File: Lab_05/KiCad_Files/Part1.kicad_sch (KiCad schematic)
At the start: 9 parts, among them Q10 NPN

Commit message: Continue Lab 5
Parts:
- added R115: 100R, symbol Device:R
- added V102: 15V, symbol Simulation_SPICE:VDC
- C103: renamed from C3; value C -> 1uF; symbol Device:C -> Device:C_Polarized_US
- C104: renamed from C4; value 40C -> 47uF; symbol Device:C -> Device:C_Polarized_US
- L101: renamed from L1; value L -> 4mH
- R116: renamed from R15; value R -> 10K
- R117: renamed from R16; value R -> 1K
- R118: renamed from R18; value 24R -> 2K7
- R119: renamed from R17; value R -> 100R
- V1: value VSIN -> VSIN_P1
- renumbered Q10 to Q110
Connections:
- net +15V: now also V102.1
- net GND: now also V102.2
- net at Q110.2 (B), R116.2, R117.1: now also C104.1; no longer C104.2
- net at C103.1, L101.1: now also C104.2, R115.2; no longer C104.1, V1.1
- new net: R115.1, V1.1
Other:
- note added: ".ac dec 100 1 10Meg"
- company: (none) -> Jim Horwitz & Mark Vaughn, Jork Incorporated
- title: (none) -> Single-Transistor Bandpass Amplifier
- moved on the sheet: L101, Q110, R116, R117, R118, R119

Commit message: Finish Saturday Schematics
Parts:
- renumbered C103 to C357, C104 to C358, L101 to L353, Q110 to Q362, R115 to R377, R116 to R378, R117 to R379, R118 to R380, R119 to R381, V102 to V353
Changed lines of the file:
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@@
   (symbol (lib_id "Device:R") (at 116.84 72.39 0) (unit 1)
     (in_bom yes) (on_board yes) (dnp no) (fields_autoplaced)
-    (property "Reference" "R117" (at 119.38 71.12 0)
+    (property "Reference" "R379" (at 119.38 71.12 0)
       (effects (font (size 1.27 1.27)) (justify left))
     )
@@
       (project "Lab05"
         (path "/9fa84b6a-7d78-4b93-9106-2eb97c609eaa/a137afc5-afed-494e-bb1a-b2a03cb8cb70"
-          (reference "R117") (unit 1)
+          (reference "R379") (unit 1)
         )
       )
@@
         )
         (path "/9fa84b6a-7d78-4b93-9106-2eb97c609eaa/a137afc5-afed-494e-bb1a-b2a03cb8cb70"
-          (reference "#PWR0126") (unit 1)
+          (reference "#PWR0389") (unit 1)
         )
       )
@@
   (symbol (lib_id "Device:R") (at 132.08 76.2 0) (unit 1)
     (in_bom yes) (on_board yes) (dnp no) (fields_autoplaced)
-    (property "Reference" "R119" (at 134.62 74.93 0)
+    (property "Reference" "R381" (at 134.62 74.93 0)
       (effects (font (size 1.27 1.27)) (justify left))
     )
@@
       (project "Lab05"
         (path "/9fa84b6a-7d78-4b93-9106-2eb97c609eaa/a137afc5-afed-494e-bb1a-b2a03cb8cb70"
-          (reference "R119") (unit 1)
+          (reference "R381") (unit 1)
         )
       )
@@
         )
         (path "/9fa84b6a-7d78-4b93-9106-2eb97c609eaa/a137afc5-afed-494e-bb1a-b2a03cb8cb70"
-          (reference "#PWR0128") (unit 1)
+          (reference "#PWR0391") (unit 1)
         )
       )
@@
         )
         (path "/9fa84b6a-7d78-4b93-9106-2eb97c609eaa/a137afc5-afed-494e-bb1a-b2a03cb8cb70"
-          (reference "V103") (unit 1)
+          (reference "V354") (unit 1)
         )
       )
@@
   (symbol (lib_id "Simulation_SPICE:VDC") (at 26.67 111.76 0) (unit 1)
     (in_bom yes) (on_board yes) (dnp no) (fields_autoplaced)
-    (property "Reference" "V102" (at 30.48 110.4542 0)
+    (property "Reference" "V353" (at 30.48 110.4542 0)
       (effects (font (size 1.27 1.27)) (justify left))
     )
@@
       (project "Lab05"
         (path "/9fa84b6a-7d78-4b93-9106-2eb97c609eaa/a137afc5-afed-494e-bb1a-b2a03cb8cb70"
-          (reference "V102") (unit 1)
+          (reference "V353") (unit 1)
         )
       )
@@
         )
         (path "/9fa84b6a-7d78-4b93-9106-2eb97c609eaa/a137afc5-afed-494e-bb1a-b2a03cb8cb70"
-          (reference "#PWR0130") (unit 1)
+          (reference "#PWR0393") (unit 1)
         )
       )
@@
         )
         (path "/9fa84b6a-7d78-4b93-9106-2eb97c609eaa/a137afc5-afed-494e-bb1a-b2a03cb8cb70"
-          (reference "#PWR0123") (unit 1)
+          (reference "#PWR0386") (unit 1)
         )
       )
@@
         )
         (path "/9fa84b6a-7d78-4b93-9106-2eb97c609eaa/a137afc5-afed-494e-bb1a-b2a03cb8cb70"
-          (reference "#PWR0124") (unit 1)
+          (reference "#PWR0387") (unit 1)
         )
       )
@@
   (symbol (lib_id "Device:R") (at 76.2 66.04 90) (unit 1)
     (in_bom yes) (on_board yes) (dnp no)
-    (property "Reference" "R115" (at 76.2 63.5 90)
+    (property "Reference" "R377" (at 76.2 63.5 90)
       (effects (font (size 1.27 1.27)))
     )
@@
       (project "Lab05"
         (path "/9fa84b6a-7d78-4b93-9106-2eb97c609eaa/a137afc5-afed-494e-bb1a-b2a03cb8cb70"
-          (reference "R115") (unit 1)
+          (reference "R377") (unit 1)
         )
       )
@@
   (symbol (lib_id "Device:C_Polarized_US") (at 96.52 72.39 0) (unit 1)
     (in_bom yes) (on_board yes) (dnp no) (fields_autoplaced)
-    (property "Reference" "C103" (at 100.33 71.12 0)
+    (property "Reference" "C357" (at 100.33 71.12 0)
       (effects (font (size 1.27 1.27)) (justify left))
     )
@@
       (project "Lab05"
         (path "/9fa84b6a-7d78-4b93-9106-2eb97c609eaa/a137afc5-afed-494e-bb1a-b2a03cb8cb70"
-          (reference "C103") (unit 1)
+          (reference "C357") (unit 1)
         )
       )
@@
   (symbol (lib_id "Device:L") (at 85.09 72.39 0) (unit 1)
     (in_bom yes) (on_board yes) (dnp no) (fields_autoplaced)
-    (property "Reference" "L101" (at 86.36 71.12 0)
+    (property "Reference" "L353" (at 86.36 71.12 0)
       (effects (font (size 1.27 1.27)) (justify left))
     )
@@
       (project "Lab05"
         (path "/9fa84b6a-7d78-4b93-9106-2eb97c609eaa/a137afc5-afed-494e-bb1a-b2a03cb8cb70"
-          (reference "L101") (unit 1)
+          (reference "L353") (unit 1)
         )
       )
@@
         )
         (path "/9fa84b6a-7d78-4b93-9106-2eb97c609eaa/a137afc5-afed-494e-bb1a-b2a03cb8cb70"
-          (reference "#PWR0125") (unit 1)
+          (reference "#PWR0388") (unit 1)
         )
       )
@@
   (symbol (lib_id "power:+15V") (at 26.67 102.87 0) (unit 1)
     (in_bom yes) (on_board yes) (dnp no) (fields_autoplaced)
-    (property "Reference" "#PWR0122" (at 26.67 106.68 0)
+    (property "Reference" "#PWR0385" (at 26.67 106.68 0)
       (effects (font (size 1.27 1.27)) hide)
     )
@@
       (project "Lab05"
         (path "/9fa84b6a-7d78-4b93-9106-2eb97c609eaa/a137afc5-afed-494e-bb1a-b2a03cb8cb70"
-          (reference "#PWR0122") (unit 1)
+          (reference "#PWR0385") (unit 1)
         )
       )
@@
   (symbol (lib_id "power:+15V") (at 116.84 52.07 0) (unit 1)
     (in_bom yes) (on_board yes) (dnp no) (fields_autoplaced)
-    (property "Reference" "#PWR0127" (at 116.84 55.88 0)
+    (property "Reference" "#PWR0390" (at 116.84 55.88 0)
       (effects (font (size 1.27 1.27)) hide)
     )
@@
       (project "Lab05"
         (path "/9fa84b6a-7d78-4b93-9106-2eb97c609eaa/a137afc5-afed-494e-bb1a-b2a03cb8cb70"
-          (reference "#PWR0127") (unit 1)
+          (reference "#PWR0390") (unit 1)
         )
       )
@@
   (symbol (lib_id "Simulation_SPICE:NPN") (at 129.54 66.04 0) (unit 1)
     (in_bom yes) (on_board yes) (dnp no) (fields_autoplaced)
-    (property "Reference" "Q110" (at 134.62 64.77 0)
+    (property "Reference" "Q362" (at 134.62 64.77 0)
       (effects (font (size 1.27 1.27)) (justify left))
     )
@@
       (project "Lab05"
         (path "/9fa84b6a-7d78-4b93-9106-2eb97c609eaa/a137afc5-afed-494e-bb1a-b2a03cb8cb70"
-          (reference "Q110") (unit 1)
+          (reference "Q362") (unit 1)
         )
       )
@@
   (symbol (lib_id "Device:C_Polarized_US") (at 107.95 66.04 270) (mirror x) (unit 1)
     (in_bom yes) (on_board yes) (dnp no)
-    (property "Reference" "C104" (at 107.95 58.42 90)
+    (property "Reference" "C358" (at 107.95 58.42 90)
       (effects (font (size 1.27 1.27)))
     )
@@
       (project "Lab05"
         (path "/9fa84b6a-7d78-4b93-9106-2eb97c609eaa/a137afc5-afed-494e-bb1a-b2a03cb8cb70"
-          (reference "C104") (unit 1)
+          (reference "C358") (unit 1)
         )
       )
@@
   (symbol (lib_id "Device:R") (at 132.08 54.61 0) (unit 1)
     (in_bom yes) (on_board yes) (dnp no) (fields_autoplaced)
-    (property "Reference" "R118" (at 134.62 53.34 0)
+    (property "Reference" "R380" (at 134.62 53.34 0)
       (effects (font (size 1.27 1.27)) (justify left))
     )
@@
       (project "Lab05"
         (path "/9fa84b6a-7d78-4b93-9106-2eb97c609eaa/a137afc5-afed-494e-bb1a-b2a03cb8cb70"
-          (reference "R118") (unit 1)
+          (reference "R380") (unit 1)
         )
       )
@@
   (symbol (lib_id "Device:R") (at 116.84 57.15 0) (unit 1)
     (in_bom yes) (on_board yes) (dnp no) (fields_autoplaced)
-    (property "Reference" "R116" (at 119.38 55.88 0)
+    (property "Reference" "R378" (at 119.38 55.88 0)
       (effects (font (size 1.27 1.27)) (justify left))
     )
@@
       (project "Lab05"
         (path "/9fa84b6a-7d78-4b93-9106-2eb97c609eaa/a137afc5-afed-494e-bb1a-b2a03cb8cb70"
-          (reference "R116") (unit 1)
+          (reference "R378") (unit 1)
         )
       )
@@
   (symbol (lib_id "power:+15V") (at 132.08 49.53 0) (unit 1)
     (in_bom yes) (on_board yes) (dnp no) (fields_autoplaced)
-    (property "Reference" "#PWR0129" (at 132.08 53.34 0)
+    (property "Reference" "#PWR0392" (at 132.08 53.34 0)
       (effects (font (size 1.27 1.27)) hide)
     )
@@
       (project "Lab05"
         (path "/9fa84b6a-7d78-4b93-9106-2eb97c609eaa/a137afc5-afed-494e-bb1a-b2a03cb8cb70"
-          (reference "#PWR0129") (unit 1)
-        )
-      )
+          (reference "#PWR0392") (unit 1)
+        )
+      )

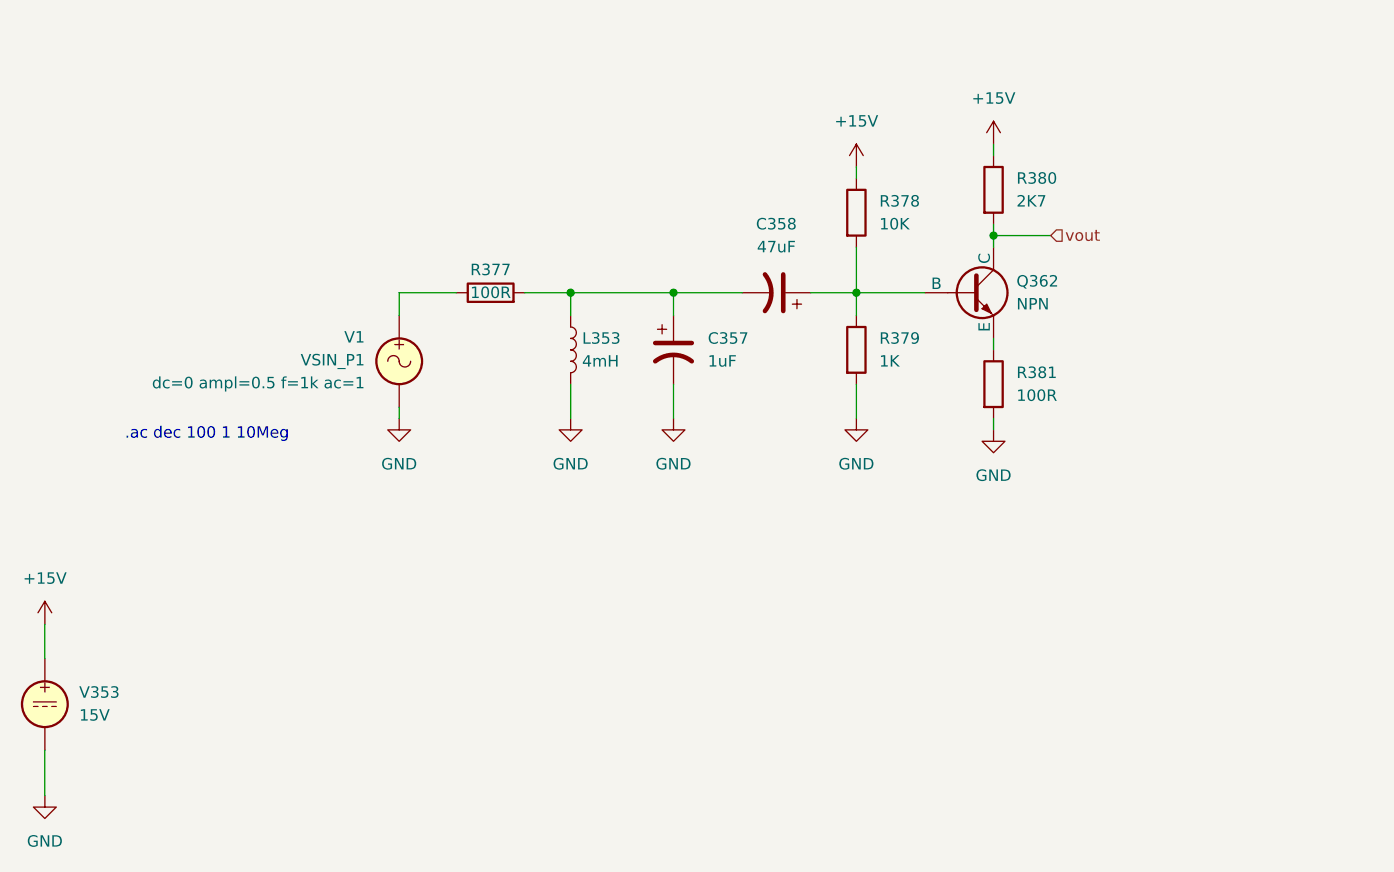
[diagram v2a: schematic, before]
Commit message: Revise part 3 Version 1
For next revision:
- add collector resistor to Q304
- remove R309
- add emitter follower after integrator
For the future:
- add more poles to bandpass!!
- maybe a resonant filter?
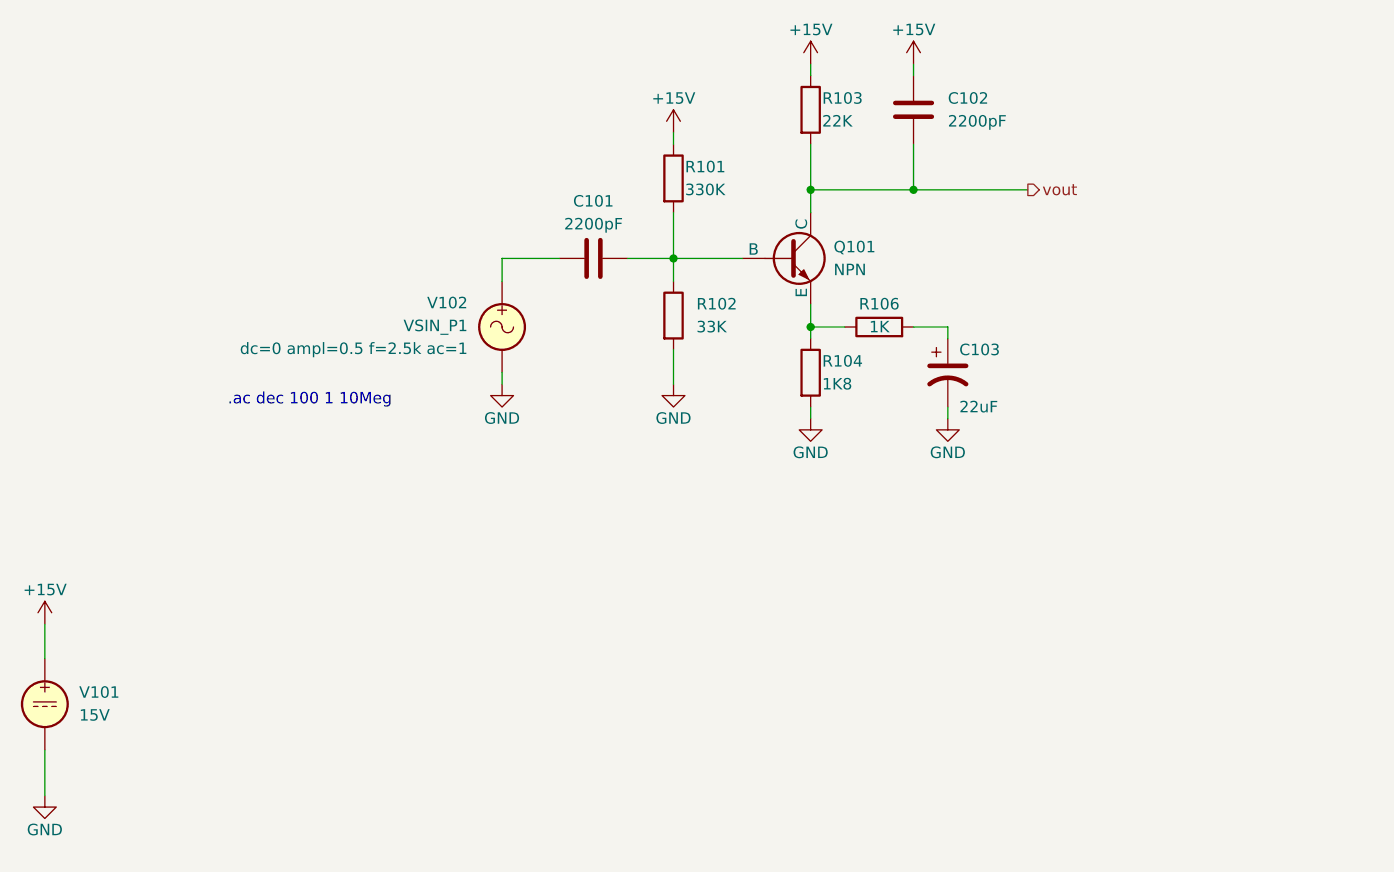
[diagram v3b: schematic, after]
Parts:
- removed C357: 1uF, symbol Device:C_Polarized_US
- removed C358: 47uF, symbol Device:C_Polarized_US
- removed L353: 4mH, symbol Device:L
- removed R377: 100R, symbol Device:R
- added C101, C102: 2200pF, symbol Device:C
- added C103: 22uF, symbol Device:C_Polarized_US
- added R106: 1K, symbol Device:R
- R101: renamed from R378; value 10K -> 330K
- R102: renamed from R379; value 1K -> 33K
- R103: renamed from R380; value 2K7 -> 22K
- R104: renamed from R381; value 100R -> 1K8
- renumbered Q362 to Q101, V353 to V101, V1 to V102
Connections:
- net +15V: now also C102.1
- net GND: now also C103.2
- net vout: now also C102.2
- net at Q101.2 (B), R101.2, R102.1: now also C101.2
- net at Q101.3 (E), R104.1: now also R106.1
- net at V102.1: now also C101.1
- new net: C103.1, R106.2
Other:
- moved on the sheet: Q101, R101, R102, R103, R104, V102

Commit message: Finish Lab 5
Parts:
- R103: value 22K -> 18K
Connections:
- net +15V: no longer C102.1
- net GND: now also C102.2
- net vout: now also C102.1; no longer C102.2
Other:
- moved on the sheet: C102
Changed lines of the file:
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@@
   (junction (at 96.52 62.23) (diameter 0) (color 0 0 0 0)
   )
-  (junction (at 123.19 54.61) (diameter 0) (color 0 0 0 0)
+  (junction (at 134.62 54.61) (diameter 0) (color 0 0 0 0)
   )
   (junction (at 111.76 69.85) (diameter 0) (color 0 0 0 0)
@@
     (stroke (width 0) (type default))
   )
+  (wire (pts (xy 134.62 54.61) (xy 144.78 54.61))
+    (stroke (width 0) (type default))
+  )
   (wire (pts (xy 77.47 64.77) (xy 77.47 62.23))
     (stroke (width 0) (type default))
@@
     (stroke (width 0) (type default))
   )
-  (wire (pts (xy 123.19 49.53) (xy 123.19 54.61))
-    (stroke (width 0) (type default))
-  )
   (wire (pts (xy 96.52 72.39) (xy 96.52 76.2))
     (stroke (width 0) (type default))
   )
-  (wire (pts (xy 111.76 54.61) (xy 123.19 54.61))
-    (stroke (width 0) (type default))
-  )
-  (wire (pts (xy 123.19 40.64) (xy 123.19 41.91))
-    (stroke (width 0) (type default))
-  )
   (wire (pts (xy 96.52 62.23) (xy 96.52 64.77))
     (stroke (width 0) (type default))
@@
     (stroke (width 0) (type default))
   )
+  (wire (pts (xy 134.62 54.61) (xy 134.62 55.88))
+    (stroke (width 0) (type default))
+  )
   (wire (pts (xy 111.76 40.64) (xy 111.76 41.91))
     (stroke (width 0) (type default))
   )
-  (wire (pts (xy 123.19 54.61) (xy 135.89 54.61))
+  (wire (pts (xy 111.76 54.61) (xy 134.62 54.61))
     (stroke (width 0) (type default))
   )
@@
     (effects (font (size 1.27 1.27)) (justify left bottom))
   )
-  (hierarchical_label "vout" (shape output) (at 135.89 54.61 0) (fields_autoplaced)
+  (hierarchical_label "vout" (shape output) (at 144.78 54.61 0) (fields_autoplaced)
     (effects (font (size 1.27 1.27)) (justify left))
   )
@@
     )
   )
-  (symbol (lib_id "power:+15V") (at 123.19 40.64 0) (unit 1)
-    (in_bom yes) (on_board yes) (dnp no)
-    (property "Reference" "#PWR0108" (at 123.19 44.45 0)
-      (effects (font (size 1.27 1.27)) hide)
-    )
-    (property "Value" "+15V" (at 123.19 36.83 0)
-      (effects (font (size 1.27 1.27)))
-    )
-    (property "Footprint" "" (at 123.19 40.64 0)
-      (effects (font (size 1.27 1.27)) hide)
-    )
-    (property "Datasheet" "" (at 123.19 40.64 0)
-      (effects (font (size 1.27 1.27)) hide)
-    )
-    (pin "1")
-    (instances
-      (project "Lab05"
-        (path "/9fa84b6a-7d78-4b93-9106-2eb97c609eaa/a137afc5-afed-494e-bb1a-b2a03cb8cb70"
-          (reference "#PWR0108") (unit 1)
-        )
-      )
-    )
-  )
   (symbol (lib_id "Device:R") (at 119.38 69.85 90) (unit 1)
     (in_bom yes) (on_board yes) (dnp no)
@@
     )
   )
-  (symbol (lib_id "Device:C") (at 123.19 45.72 0) (unit 1)
+  (symbol (lib_id "Device:C") (at 134.62 59.69 0) (unit 1)
     (in_bom yes) (on_board yes) (dnp no) (fields_autoplaced)
-    (property "Reference" "C102" (at 127 44.45 0)
-      (effects (font (size 1.27 1.27)) (justify left))
-    )
-    (property "Value" "2200pF" (at 127 46.99 0)
-      (effects (font (size 1.27 1.27)) (justify left))
-    )
-    (property "Footprint" "" (at 124.1552 49.53 0)
-      (effects (font (size 1.27 1.27)) hide)
-    )
-    (property "Datasheet" "~" (at 123.19 45.72 0)
+    (property "Reference" "C102" (at 138.43 58.42 0)
+      (effects (font (size 1.27 1.27)) (justify left))
+    )
+    (property "Value" "2200pF" (at 138.43 60.96 0)
+      (effects (font (size 1.27 1.27)) (justify left))
+    )
+    (property "Footprint" "" (at 135.5852 63.5 0)
+      (effects (font (size 1.27 1.27)) hide)
+    )
+    (property "Datasheet" "~" (at 134.62 59.69 0)
       (effects (font (size 1.27 1.27)) hide)
     )
@@
       (effects (font (size 1.27 1.27)) hide)
     )
-    (property "Value" "+15V" (at 26.67 99.06 0)
+    (property "Value" "+15V" (at 26.67 99.314 0)
       (effects (font (size 1.27 1.27)))
     )
@@
       (effects (font (size 1.27 1.27)) hide)
     )
-    (property "Value" "+15V" (at 96.52 44.45 0)
+    (property "Value" "+15V" (at 96.52 44.704 0)
       (effects (font (size 1.27 1.27)))
     )
@@
       (effects (font (size 1.27 1.27)) (justify left))
     )
-    (property "Value" "22K" (at 113.03 46.99 0)
+    (property "Value" "18K" (at 113.03 46.99 0)
       (effects (font (size 1.27 1.27)) (justify left))
     )
@@
     )
   )
+  (symbol (lib_id "power:GND") (at 134.62 63.5 0) (unit 1)
+    (in_bom yes) (on_board yes) (dnp no)
+    (property "Reference" "#PWR0317" (at 134.62 69.85 0)
+      (effects (font (size 1.27 1.27)) hide)
+    )
+    (property "Value" "GND" (at 134.62 67.31 0)
+      (effects (font (size 1.27 1.27)))
+    )
+    (property "Footprint" "" (at 134.62 63.5 0)
+      (effects (font (size 1.27 1.27)) hide)
+    )
+    (property "Datasheet" "" (at 134.62 63.5 0)
+      (effects (font (size 1.27 1.27)) hide)
+    )
+    (pin "1")
+    (instances
+      (project "Lab05"
+        (path "/9fa84b6a-7d78-4b93-9106-2eb97c609eaa/a137afc5-afed-494e-bb1a-b2a03cb8cb70"
+          (reference "#PWR0317") (unit 1)
+        )
+      )
+    )
+  )
   (symbol (lib_id "Device:R") (at 96.52 53.34 0) (unit 1)
     (in_bom yes) (on_board yes) (dnp no)
@@
       (effects (font (size 1.27 1.27)) hide)
     )
-    (property "Value" "+15V" (at 111.76 36.83 0)
-      (effects (font (size 1.27 1.27)))
-    )
+    (property "Value" "+15V" (at 111.76 37.084 0)
+      (effects (font (size 1.27 1.27)))
+    )
